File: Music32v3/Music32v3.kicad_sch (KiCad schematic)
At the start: 0 parts

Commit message: PSU update
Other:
- added sheet USB Stuff (usb_stuff.kicad_sch)
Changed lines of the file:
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@@
 (kicad_sch (version 20230121) (generator eeschema)
   (paper "A4")
+  (sheet (at 111.76 54.61) (size 16.51 8.89) (fields_autoplaced)
+    (stroke (width 0.1524) (type solid))
+    (fill (color 0 0 0 0.0000))
+    (property "Sheetname" "USB Stuff" (at 111.76 53.8984 0)
+      (effects (font (size 1.27 1.27)) (justify left bottom))
+    )
+    (property "Sheetfile" "usb_stuff.kicad_sch" (at 111.76 64.0846 0)
+      (effects (font (size 1.27 1.27)) (justify left top))
+    )
+    (instances
+      (project "Music32v3"
+        (path "/492e826b-8900-4c12-8604-1c812b2e1995" (page "4"))
+      )
+    )
+  )
   (sheet (at 86.36 54.61) (size 13.97 8.89) (fields_autoplaced)
     (stroke (width 0.1524) (type solid))

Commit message: SD card and usb and power
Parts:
- added C14, C18, C19, C45, C46: 100nF, Capacitor_SMD:C_0402_1005Metric, symbol Device:C_Small
- added C15, C16, C17, C20, C21, C22, C23, C24, C25: 1uF, Capacitor_SMD:C_0402_1005Metric, symbol Device:C_Small
- added C26: 47nF, Capacitor_SMD:C_0402_1005Metric, symbol Device:C_Small
- added C27: 4.7uF, Capacitor_SMD:C_0402_1005Metric, symbol Device:C_Small
- added J2: PJ-316A-6A, Footprints:PJ-316A-6A, symbol Connector_Audio:AudioJack4_SwitchT1
- added MK1: GMI4015P-2C-66db, Footprints:GMI4015P-2C-66db, symbol Device:Microphone
- added R11, R12, R19, R20: 2K, Resistor_SMD:R_0402_1005Metric, symbol Device:R
- added R13, R14: 10K, Resistor_SMD:R_0402_1005Metric, symbol Device:R
- added R15, R16: 220R, Resistor_SMD:R_0402_1005Metric, symbol Device:R
- added R17, R36: 1M, Resistor_SMD:R_0402_1005Metric, symbol Device:R
- added R18, R21: 33R, Resistor_SMD:R_0402_1005Metric, symbol Device:R
- added R35: 10R, Resistor_SMD:R_0402_1005Metric, symbol Device:R
- added U3: ES8327, Package_DFN_QFN:QFN-32-1EP_4x4mm_P0.4mm_EP2.9x2.9mm_ThermalVias, symbol Audio:ES8327
- added U8: ST7889 2" LCD, Footprints:TFT020-2_same_side, symbol Lcd:2{dblquote}_IPS_LCD_ST7889
- added U9: MAX17048, Package_DFN_QFN:DFN-8-1EP_2x2mm_P0.5mm_EP0.8x1.6mm, symbol OSSG_components_lib:MAX17048
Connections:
- new net: C25.2, U3.17 (CPVSSP)
- new net: C20.2, U3.12 (CPTOP)
- new net: C20.1, U3.16 (CPBOT)
- new net: R21.1, U3.18 (ROUT)
- new net: R18.1, U3.19 (LOUT)
- new net: C16.2, U3.20 (DACVREF)
- new net: C17.2, U3.24 (VMID)
- new net: C24.2, U3.25 (MIC1N)
- new net: C23.2, U3.26 (MIC1P)
- new net: C22.2, U3.27 (MIC2N)
- new net: C21.2, U3.28 (MIC2P)
- new net: R13.2, U3.30 (CE)
- new net: C26.2, R15.2, U3.9 (HEADSET)
- new net: J2.R1, R21.2
- new net: J2.T, R18.2
- new net: C27.2, R16.2, R19.1
- new net: R35.2, U8.3 (LEDA)
- new net +1V8: C19.2, U3.11 (CPVDD)
- new net +3.3V: C14.2, C45.1, R11.1, R12.1, R14.1, R17.1, R35.1, R36.2, U3.2 (DVDD), U3.3 (PVDD), U8.4 (VCC)
- new net +3.3VA: C18.2, U3.21 (AVDD)
- new net ADCVREF: C15.2, R16.1, U3.23 (ADCVREF)
- new net BATT+: C46.1, U9.2 (CELL), U9.3 (Vdd)
- new net CLK: U8.9 (SCL)
- new net DISPLAY_CS: U8.8 (CS)
- new net DISPLAY_DC: U8.7 (D/C)
- new net DISPLAY_RESET: R36.1, U8.11 (RESET)
- new net FUEL_INT: U9.5 (ALRT)
- new net GND: C14.1, C15.1, C16.1, C17.1, C18.1, C19.1, C25.1, C26.1, C27.1, C45.2, C46.2, R13.1, R20.2, U3.14 (CPGND), U3.22 (AGND), U3.33 (PAD), U3.4 (DGND), U8.1 (GND), U8.12 (GND), U8.5 (GND), U8.6 (GND), U9.1 (CTG), U9.4 (GND), U9.6 (QSTRT), U9.9 (EP)
- new net HEADSET_INT: R14.2, U3.10 (INOUT)
- new net HP_Detect: J2.TN, R15.1, R17.2
- new net LRCK: U3.7 (LRCK)
- new net M1+: C23.1, J2.S, U3.15 (GMS1)
- new net M1-: C24.1, J2.R2, U3.13 (GMS0)
- new net M2+: C21.1, MK1.2 (+), R19.2
- new net M2-: C22.1, MK1.1 (-), R20.1
- new net MCLK: U3.1 (MCLK)
- new net MOSI: U8.10 (SDA)
- new net SCL: R12.2, U3.32 (CCLK), U9.7 (SCL)
- new net SCLK: U3.5 (SCLK)
- new net SDA: R11.2, U3.31 (CDATA), U9.8 (SDA)
- new net SDIN: U3.6 (SDIN)
- new net SDOUT: U3.8 (SDOUT)
- no-connect marks 0 -> 1
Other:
- note added: "2" IPS LCD"
- note added: "Add:0110110"
- note added: "Class 1 caps"
- note added: "Fuel guage"
- note added: "I2S ADC/DAC"
- note added: "Same Gnd"
- note added: "add headphone interrupt"

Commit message: Schematic
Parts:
- removed C14, C18, C19: 100nF, Capacitor_SMD:C_0402_1005Metric, symbol Device:C_Small
- removed C15, C16, C17, C20, C21, C22, C23, C24, C25: 1uF, Capacitor_SMD:C_0402_1005Metric, symbol Device:C_Small
- removed C26: 47nF, Capacitor_SMD:C_0402_1005Metric, symbol Device:C_Small
- removed C27: 4.7uF, Capacitor_SMD:C_0402_1005Metric, symbol Device:C_Small
- removed J2: PJ-316A-6A, Footprints:PJ-316A-6A, symbol Connector_Audio:AudioJack4_SwitchT1
- removed MK1: GMI4015P-2C-66db, Footprints:GMI4015P-2C-66db, symbol Device:Microphone
- removed R11, R12, R19, R20: 2K, Resistor_SMD:R_0402_1005Metric, symbol Device:R
- removed R13, R14: 10K, Resistor_SMD:R_0402_1005Metric, symbol Device:R
- removed R15, R16: 220R, Resistor_SMD:R_0402_1005Metric, symbol Device:R
- removed R17: 1M, Resistor_SMD:R_0402_1005Metric, symbol Device:R
- removed R18, R21: 33R, Resistor_SMD:R_0402_1005Metric, symbol Device:R
- removed U3: ES8327, Package_DFN_QFN:QFN-32-1EP_4x4mm_P0.4mm_EP2.9x2.9mm_ThermalVias, symbol Audio:ES8327
- added Q2: CJ3134K KF, Package_TO_SOT_SMD:SOT-723, symbol Device:Q_NMOS_GSD
- added R35, R36 (x3): 1M, Resistor_SMD:R_0402_1005Metric, symbol Device:R
- added U22: SRGP400200, Music:SRGP400200_ALPS, symbol srgp400200:SRGP400200
- C45, C46: value 100nF -> 1uF
- U8: footprint Footprints:TFT020-2_same_side -> Music:TFT020-2_same_side
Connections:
- net +3.3V: now also R36.2, R36.2, R36.2
- net FUEL_INT: now also R36.1
- net GND: now also Q2.2 (S), R35.1, U22.2 (C), U22.6 (GND)
- net at U8.2 (LEDK): now also Q2.3 (D)
- net MOSI renamed MOSI_UC
- new net BL_EN: Q2.1 (G), R35.2
- new net ENCODER_1: R36.1, U22.1, U22.5 (1)
- new net ENCODER_2: R36.1, U22.3 (2), U22.4 (2)
- no-connect marks 1 -> 0
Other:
- added sheet Codec (codec.kicad_sch)
- note removed: "Class 1 caps"
- note removed: "I2S ADC/DAC"
- note removed: "Same Gnd"
- note removed: "add headphone interrupt"

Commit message: Reorganised
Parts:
- added R12 (x6): 2K, Resistor_SMD:R_0402_1005Metric, symbol Device:R
- added R13 (x4): 10K, Resistor_SMD:R_0402_1005Metric, symbol Device:R
- added R17 (x2): 1M, Resistor_SMD:R_0402_1005Metric, symbol Device:R
- added SW3: PP, Music:TS3315A, symbol Switch:SW_Push
- added SW4: RW, Music:TS3315A, symbol Switch:SW_Push
- added SW5: FF, Music:TS3315A, symbol Switch:SW_Push
- added SW6: HOME, Music:TS3315A, symbol Switch:SW_Push
- added SW7, SW8: Vol+, Music:TSA002A3816B04, symbol Switch:SW_Push
- added SW9: Select, Music:TS3315A, symbol Switch:SW_Push
- added U1: Sk-3393, Music:SK-3393M-G1, symbol sk-3393m-g1:_SK-3393M-G1
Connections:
- net +3.3V: now also R17.1, SW3.2, SW4.2, SW5.2, SW6.2, SW7.2, SW8.2
- net GND: now also R13.1, R17.1, SW9.2, U1.1, U1.6,7
- new net: R13.2, R13.2, SW7.1
- new net: R12.1, SW4.1
- new net: R12.1, SW3.1
- new net: R12.1, R13.1, R13.1
- new net: R17.2, U1.5
- new net: R12.1, R12.1, SW5.1
- new net: R12.1, R12.2
- new net: R13.2, SW8.1
- new net BUTTONS: R12.2, R12.2, R12.2, R12.2, R12.2, R13.1, R13.2, SW6.1
- new net IO0: SW9.1
- new net PWR/HOLD: R17.2, U1.3,4
- no-connect marks 0 -> 1
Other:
- note added: "Buttons"
- note added: "Encoder"
- note added: "HOME - 3.3 - 4095 FF - 3 - 3722 RW - 2.75 - 3412 PP - 2.357 - 2924 Vol+ - 1.94 - 2406 Vol- - 1.65 - 2047"
- note added: "Hold/Power switch"
- note added: "PWR is gnd for interrupt Hold is 1.65V for adc read"
- note added: "Pullups needed for ESP input only pins"
- moved on the sheet: C45, C46, Q2, R35, R36, U22, U8, U9

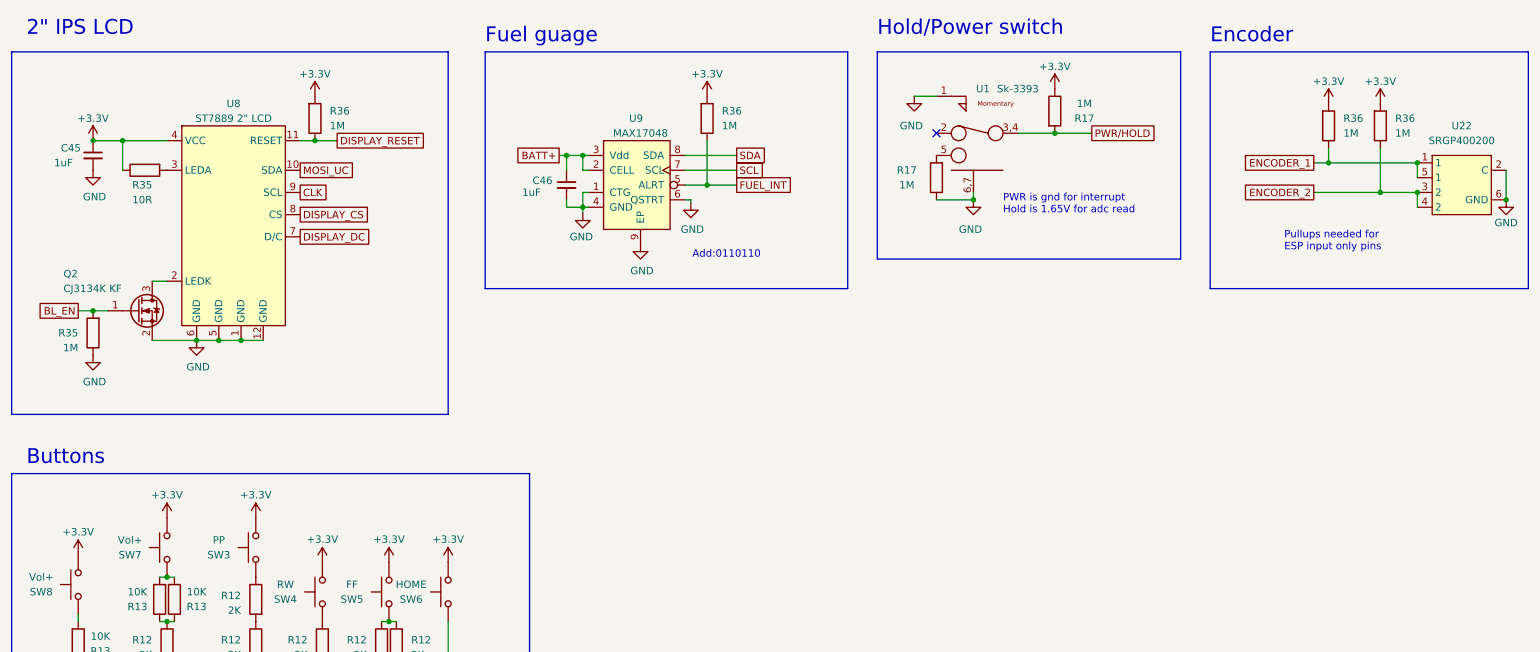
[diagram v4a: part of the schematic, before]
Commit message: PCB outline
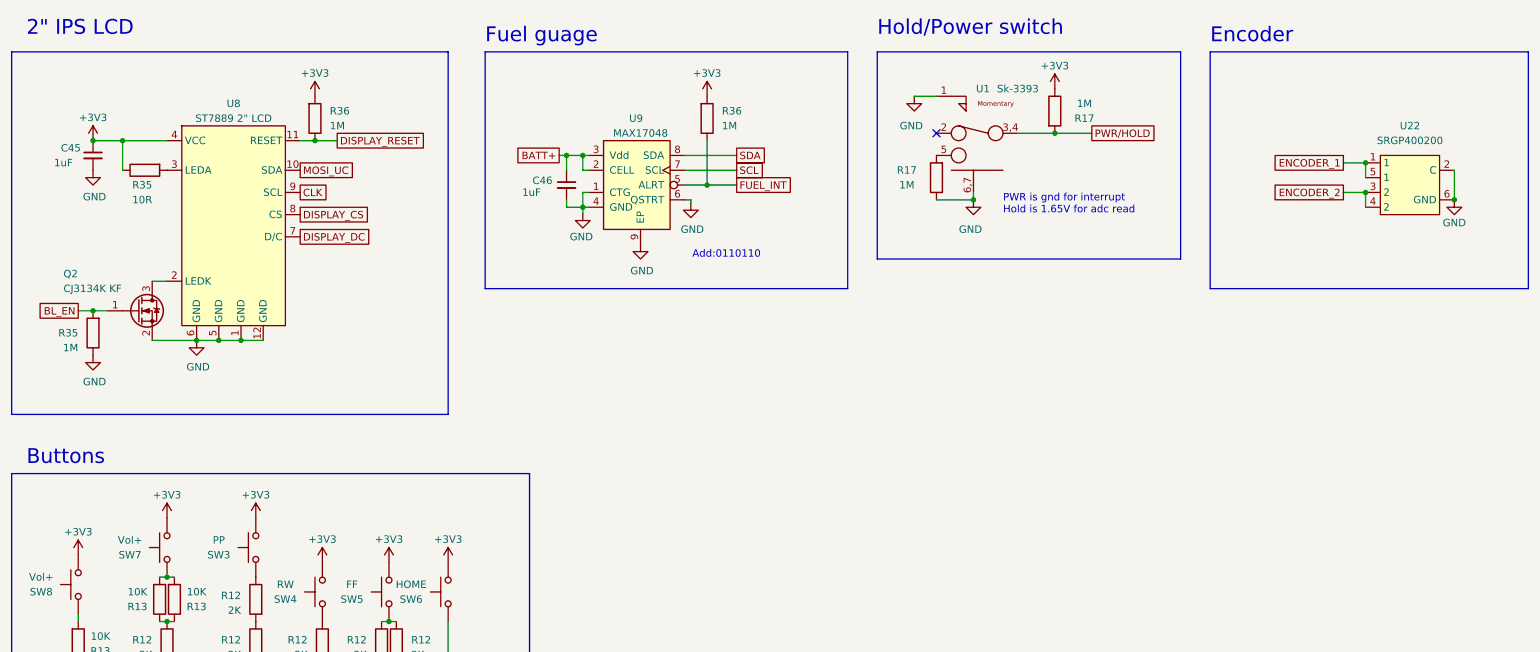
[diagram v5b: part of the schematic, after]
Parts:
- removed R36 (x2): 1M, Resistor_SMD:R_0402_1005Metric, symbol Device:R
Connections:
- net +3.3V renamed +3V3
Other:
- note removed: "Pullups needed for ESP input only pins"
- moved on the sheet: U22

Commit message: Board setup
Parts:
- removed R12 (x3): 2K, Resistor_SMD:R_0402_1005Metric, symbol Device:R
- removed R13 (x2): 10K, Resistor_SMD:R_0402_1005Metric, symbol Device:R
- added C28 (x2): 0.1uF, Capacitor_SMD:C_0402_1005Metric, symbol Device:C_Small
- added R12 (x2): 1K, Resistor_SMD:R_0402_1005Metric, symbol Device:R
- added R13: 10K, Resistor_SMD:R_0402_1005Metric, symbol Device:R
- added TP1, TP2, TP3, TP5, TP6, TP7, TP8, TP9: TestPoint, TestPoint:TestPoint_Pad_D2.0mm, symbol Connector:TestPoint
- added TP4: TestPoint, TestPoint:TestPoint_Pad_D1.5mm, symbol Connector:TestPoint
- R12: value 2K -> 1K
- R12: value 2K -> 220
- R17: value 1M -> 5.1K
- R17: value 1M -> 10K
- SW7: value Vol+ -> Vol-
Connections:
- net BL_EN: now also TP2.1
- net BUTTONS: now also C28.1, R12.2, R12.2, R13.1, TP7.1
- net DISPLAY_CS: now also TP6.1
- net DISPLAY_DC: now also TP3.1
- net DISPLAY_RESET: now also TP4.1
- net FUEL_INT: now also TP8.1
- net GND: now also C28.2, C28.2
- net IO0: now also TP1.1
- net PWR/HOLD: now also C28.1, TP9.1
- net at SW7.1: now also R12.1
- net at SW4.1: now also R12.1, R12.1
- net at SW3.1: now also R12.1
- net at R13.2, SW8.1: now also R13.2
- net CLK renamed CLK_UC
- net CLK_UC: now also TP5.1
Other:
- note added: "PWR is gnd for interrupt Hold is 1.12V for adc read"
- note removed: "HOME - 3.3 - 4095 FF - 3 - 3722 RW - 2.75 - 3412 PP - 2.357 - 2924 Vol+ - 1.94 - 2406 Vol- - 1.65 - 2047"
- note removed: "PWR is gnd for interrupt Hold is 1.65V for adc read"
- moved on the sheet: R12, R13, SW3, SW4, SW5, SW6, SW7, SW8, SW9

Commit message: Fixed resistor
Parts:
- R13: value 10K -> 1K
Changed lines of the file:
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@@
       (effects (font (size 1.27 1.27)))
     )
-    (property "Value" "10K" (at 92.71 138.43 0)
+    (property "Value" "1K" (at 92.71 138.43 0)
       (effects (font (size 1.27 1.27)))
     )
